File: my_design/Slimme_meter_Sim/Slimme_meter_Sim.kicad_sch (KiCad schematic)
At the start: 0 parts

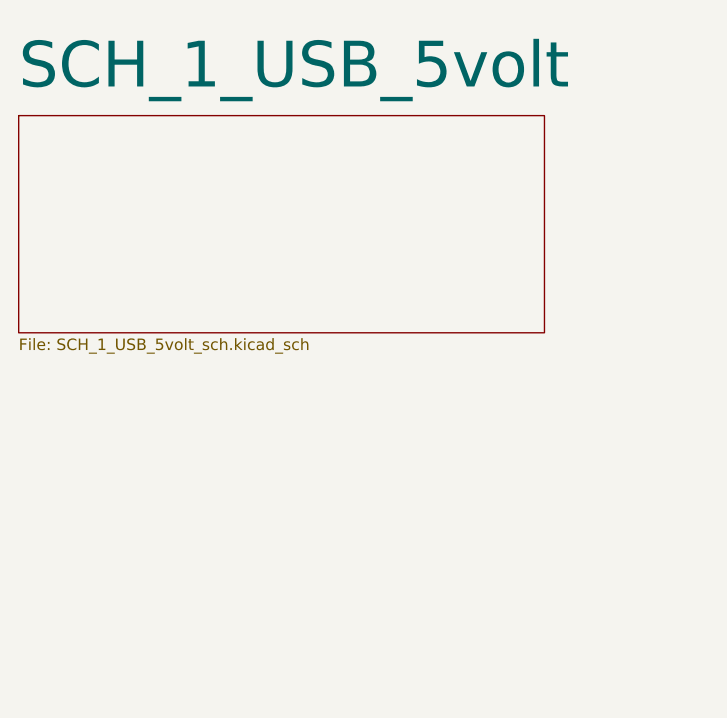
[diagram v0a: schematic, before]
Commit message: Add sheet-2 power/MCU schematic progress and document P1 opto domains.
Captures TPS26625, SY8088 3V3, ESP32-C3, RJ12 placement, and README guidance that Request/Data optos keep UART on 3.3 V while pin 5 stays open-collector on the 5 V P1 side.

Co-authored-by: Cursor <cursoragent@cursor.com>
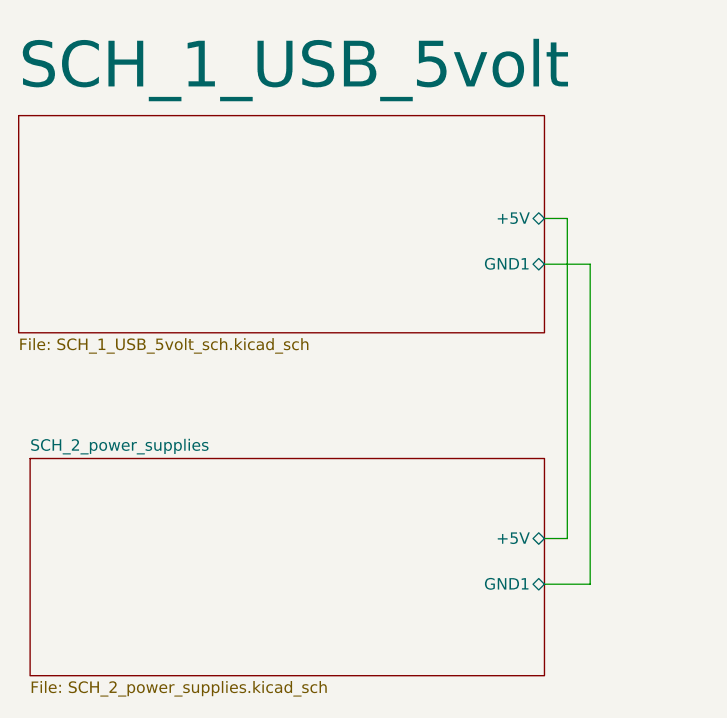
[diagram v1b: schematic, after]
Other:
- added sheet SCH_2_power_supplies (SCH_2_power_supplies.kicad_sch)
- sheet SCH_1_USB_5volt ports: added +5V, GND1; removed none
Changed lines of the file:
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@@
 		(date "2026-07-30")
+	)
+	(wire
+		(pts
+			(xy 99.06 40.64) (xy 101.6 40.64)
+		)
+		(stroke
+			(width 0)
+			(type default)
+		)
+	)
+	(wire
+		(pts
+			(xy 99.06 45.72) (xy 104.14 45.72)
+		)
+		(stroke
+			(width 0)
+			(type default)
+		)
+	)
+	(wire
+		(pts
+			(xy 99.06 76.2) (xy 101.6 76.2)
+		)
+		(stroke
+			(width 0)
+			(type default)
+		)
+	)
+	(wire
+		(pts
+			(xy 101.6 40.64) (xy 101.6 76.2)
+		)
+		(stroke
+			(width 0)
+			(type default)
+		)
+	)
+	(wire
+		(pts
+			(xy 104.14 45.72) (xy 104.14 81.28)
+		)
+		(stroke
+			(width 0)
+			(type default)
+		)
+	)
+	(wire
+		(pts
+			(xy 104.14 81.28) (xy 99.06 81.28)
+		)
+		(stroke
+			(width 0)
+			(type default)
+		)
 	)
 	(sheet
@@
 			)
 		)
+		(pin "+5V" bidirectional
+			(at 99.06 40.64 0)
+			(effects
+				(font
+					(size 1.27 1.27)
+				)
+				(justify right)
+			)
+		)
+		(pin "GND1" bidirectional
+			(at 99.06 45.72 0)
+			(effects
+				(font
+					(size 1.27 1.27)
+				)
+				(justify right)
+			)
+		)
 		(instances
 			(project "Slimme_meter_Sim"
@@
 				)
 			)
+		)
+	)
+	(sheet
+		(at 41.91 67.31)
+		(size 57.15 24.13)
+		(exclude_from_sim no)
+		(in_bom yes)
+		(on_board yes)
+		(dnp no)
+		(fields_autoplaced yes)
+		(stroke
+			(width 0.1524)
+			(type solid)
+		)
+		(fill
+			(color 0 0 0 0.0000)
+		)
+		(property "Sheetname" "SCH_2_power_supplies"
+			(at 41.91 66.5984 0)
+			(effects
+				(font
+					(size 1.27 1.27)
+				)
+				(justify left bottom)
+			)
+		)
+		(property "Sheetfile" "SCH_2_power_supplies.kicad_sch"
+			(at 41.91 92.0246 0)
+			(effects
+				(font
+					(size 1.27 1.27)
+				)
+				(justify left top)
+			)
+		)
+		(pin "+5V" bidirectional
+			(at 99.06 76.2 0)
+			(effects
+				(font
+					(size 1.27 1.27)
+				)
+				(justify right)
+			)
+		)
+		(pin "GND1" bidirectional
+			(at 99.06 81.28 0)
+			(effects
+				(font
+					(size 1.27 1.27)
+				)
+				(justify right)
+			)
+		)
+		(instances
+			(project "Slimme_meter_Sim"
+				(path "/d59de98b-abe3-4329-b084-e6d28a71ec22"
+					(page "3")
+				)
+			)

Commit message: Save KiCad schematic/PCB progress and park Pi next-step ideas.
Document assembly (stencil + hot air) and the dual-domain Pi brain option so the ESP32 path can be resumed cleanly tomorrow.

Co-authored-by: Cursor <cursoragent@cursor.com>
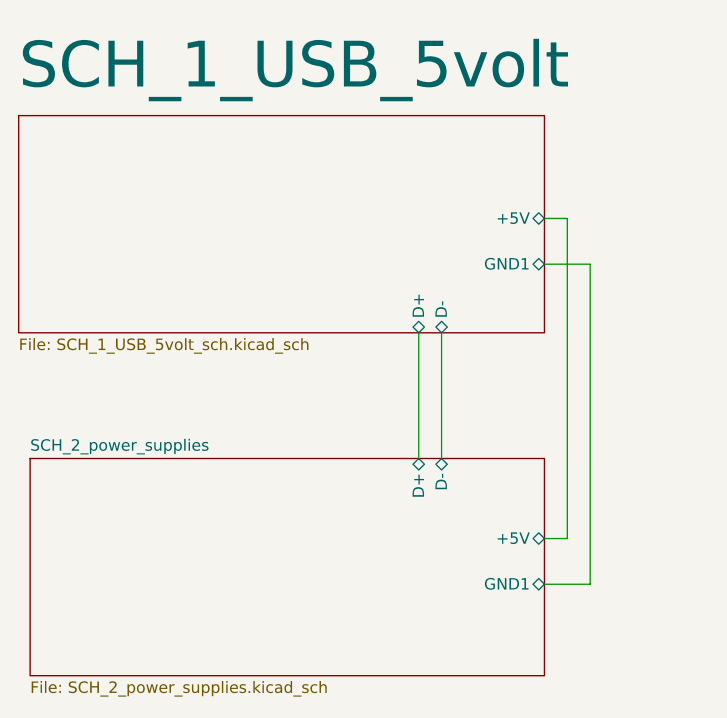
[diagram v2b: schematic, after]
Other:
- sheet SCH_1_USB_5volt ports: added D+, D-; removed none
- sheet SCH_2_power_supplies ports: added D+, D-; removed none
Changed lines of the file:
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@@
+	(wire
+		(pts
+			(xy 85.09 53.34) (xy 85.09 67.31)
+		)
+		(stroke
+			(width 0)
+			(type default)
+		)
+	)
 	(wire
 		(pts
 			(xy 101.6 40.64) (xy 101.6 76.2)
+		)
+		(stroke
+			(width 0)
+			(type default)
+		)
+	)
+	(wire
+		(pts
+			(xy 87.63 53.34) (xy 87.63 67.31)
 		)
 		(stroke
@@
 			)
 		)
+		(pin "D+" bidirectional
+			(at 85.09 53.34 270)
+			(effects
+				(font
+					(size 1.27 1.27)
+				)
+				(justify left)
+			)
+		)
+		(pin "D-" bidirectional
+			(at 87.63 53.34 270)
+			(effects
+				(font
+					(size 1.27 1.27)
+				)
+				(justify left)
+			)
+		)
 		(instances
 			(project "Slimme_meter_Sim"
@@
 			(effects
 				(font
+					(size 1.27 1.27)
+				)
+				(justify right)
+			)
+		)
+		(pin "D+" bidirectional
+			(at 85.09 67.31 90)
+			(effects
+				(font
+					(size 1.27 1.27)
+				)
+				(justify right)
+			)
+		)
+		(pin "D-" bidirectional
+			(at 87.63 67.31 90)
+			(effects
+				(font

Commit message: Save Slimme_meter_Sim KiCad progress: PCB/schematic, footprints, and firmware pin map.
Co-authored-by: Cursor <cursoragent@cursor.com>
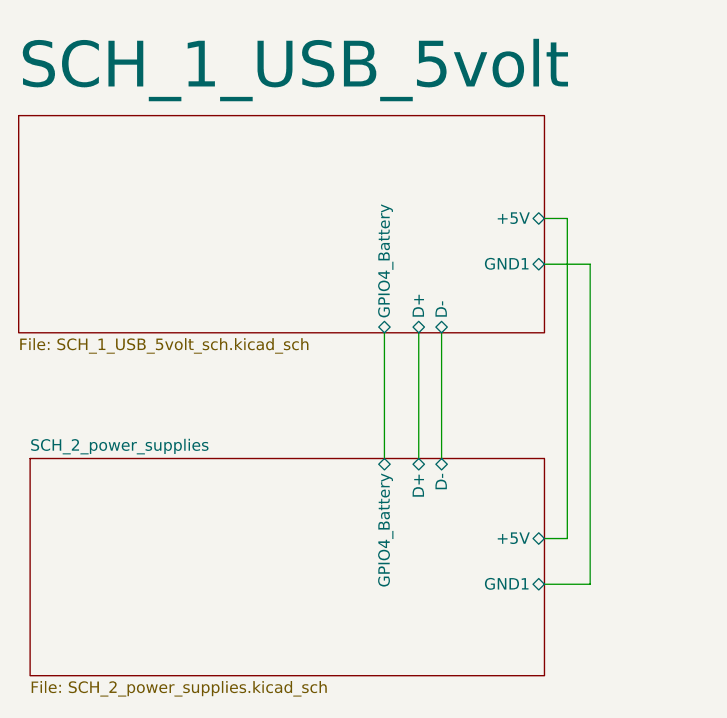
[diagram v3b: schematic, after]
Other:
- sheet SCH_1_USB_5volt ports: added GPIO4_Battery; removed none
- sheet SCH_2_power_supplies ports: added GPIO4_Battery; removed none
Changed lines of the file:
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@@
+	(wire
+		(pts
+			(xy 81.28 53.34) (xy 81.28 67.31)
+		)
+		(stroke
+			(width 0)
+			(type default)
+		)
+	)
 	(wire
 		(pts
@@
 			)
 		)
+		(pin "GPIO4_Battery" bidirectional
+			(at 81.28 53.34 270)
+			(effects
+				(font
+					(size 1.27 1.27)
+				)
+				(justify left)
+			)
+		)
 		(instances
 			(project "Slimme_meter_Sim"
@@
 			(effects
 				(font
+					(size 1.27 1.27)
+				)
+				(justify right)
+			)
+		)
+		(pin "GPIO4_Battery" bidirectional
+			(at 81.28 67.31 90)
+			(effects
+				(font
